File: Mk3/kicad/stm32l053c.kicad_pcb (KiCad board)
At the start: 2 copper layers, 26.7 x 43.2 mm, 34 parts, among them J2 GND, J3 TX, P1 SWD, U1 AP2112, U2 STM32L053C8_LQFP48, U3 ADS1015, U4 UFL_SMA, U5 RFM92/95

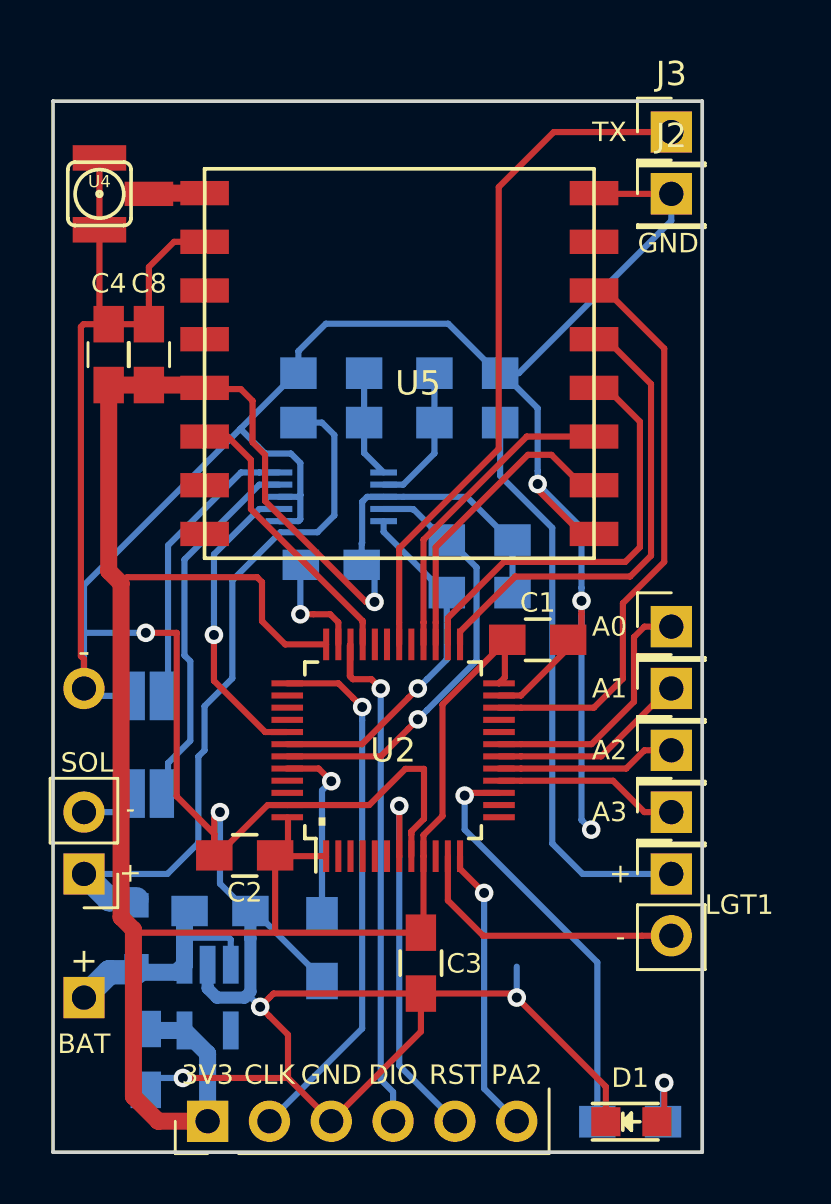
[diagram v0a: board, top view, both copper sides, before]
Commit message: More ground pins
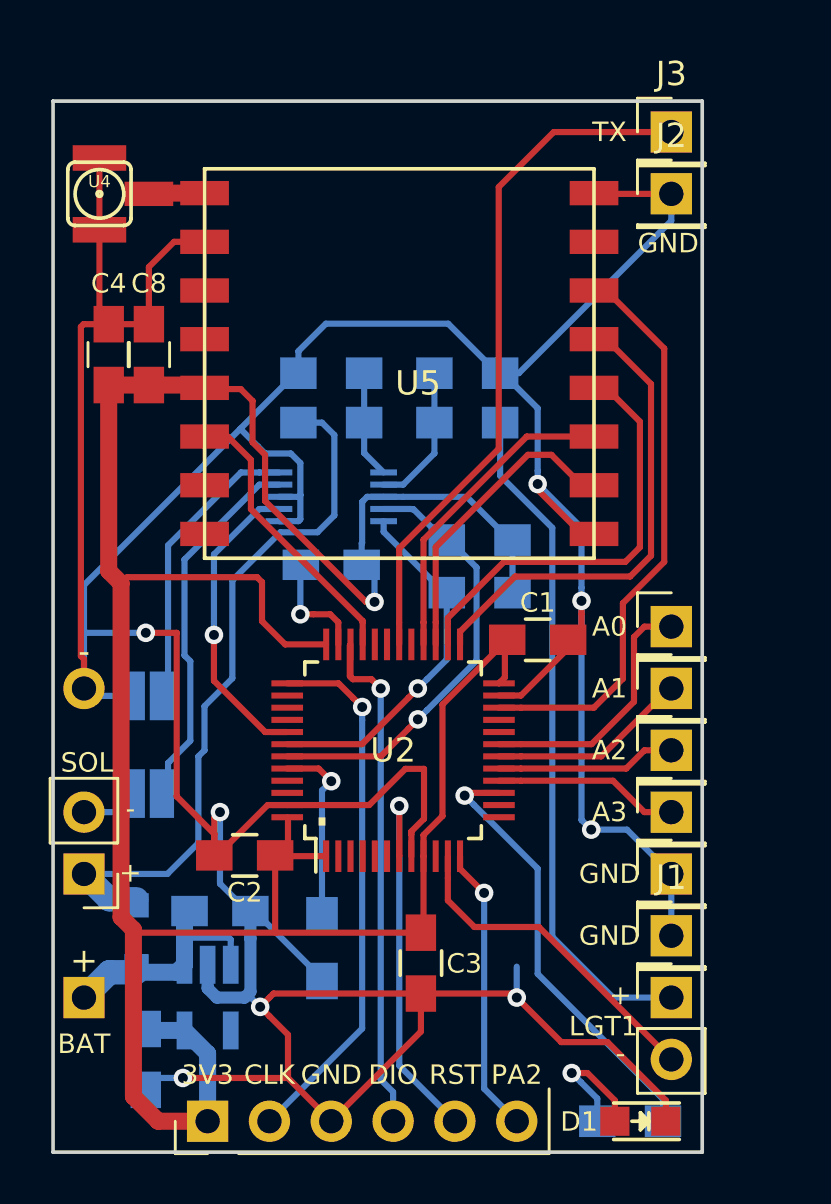
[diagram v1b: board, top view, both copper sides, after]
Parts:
- added J1: GND, Pin_Headers:Pin_Header_Straight_1x01_Pitch2.54mm, F.Cu at (161.3, 86.4)
- added J4: GND, Pin_Headers:Pin_Header_Straight_1x01_Pitch2.54mm, F.Cu at (161.3, 83.8)
- moved LGT1 5.08 mm to (161.3, 88.9)
- moved D1 0.37 mm to (160.0, 94.0), turned to 180 degrees
- turned R1 to 180 degrees
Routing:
- net Earth: track 201.8 -> 210.5 mm
- net Net-(LGT1-Pad1): track 23.6 -> 27.9 mm
- net Net-(D1-Pad2): track 3.35 -> 5.51 mm
- net LGT_GND: track 11.6 -> 13.7 mm
- net LED: track 17.1 -> 18.2 mm

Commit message: Connect all the pins of the RFM95 module
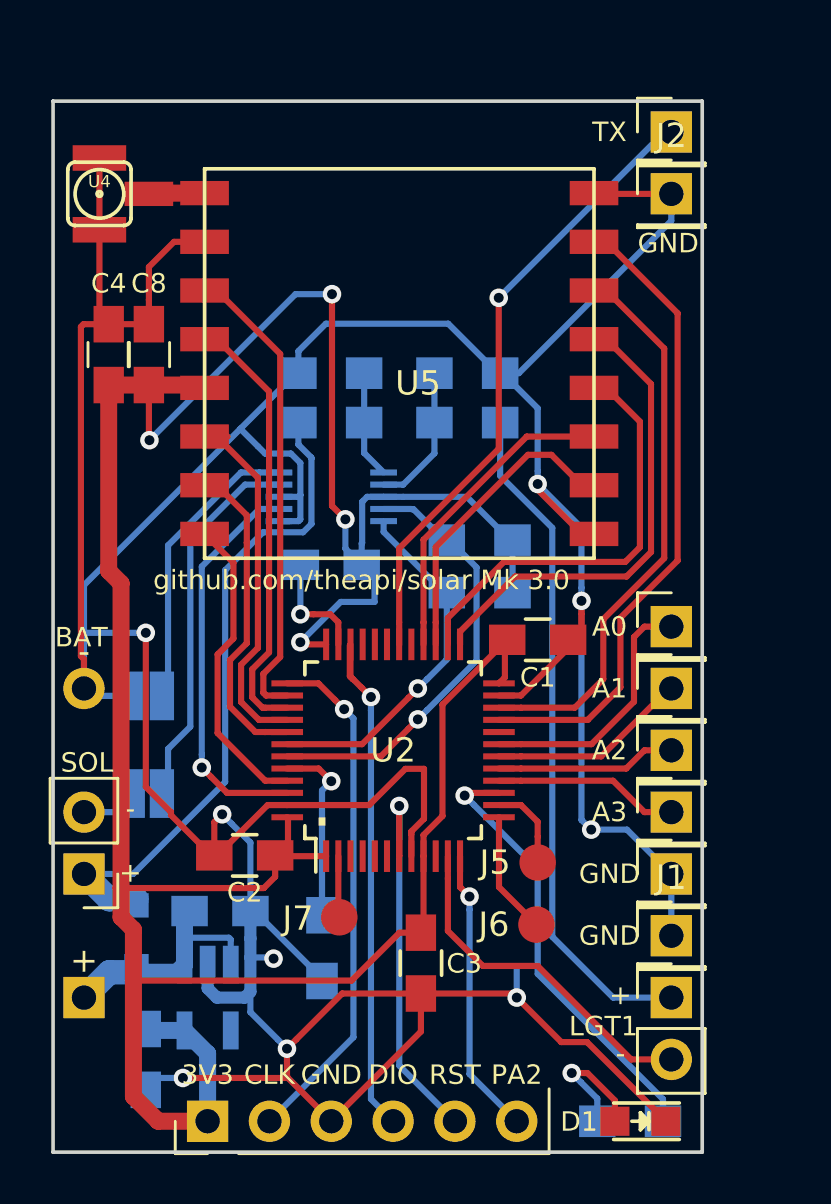
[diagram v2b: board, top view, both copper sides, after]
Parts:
- added J5: TEST_1P, theapi:TestPoint, F.Cu at (155.8, 83.3)
- added J6: TEST_1P, theapi:TestPoint, F.Cu at (155.8, 85.9)
- added J7: TEST_1P, theapi:TestPoint, F.Cu at (147.7, 85.6)
- added REF**: TheApiLogoTiny, theapi:TheApiLogoTiny, F.Cu at (137.2, 90.5)
- added REF**: TheApiLogo, theapi:TheApiLogoSmall, B.Cu at (141.8, 52.8)
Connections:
- net Net-(R4-Pad1) renamed /BOOT0
- U2 pad 13: Net-(U2-Pad13) -> /PA3
- U2 pad 14: Net-(U2-Pad14) -> /PA4
- U2 pad 2: Net-(U2-Pad2) -> /PC13
- U2 pad 21: Net-(U2-Pad21) -> DIO5
- U2 pad 33: DIO0 -> Net-(U2-Pad33)
- U2 pad 38: Net-(U2-Pad38) -> DIO3
- U2 pad 39: Net-(U2-Pad39) -> DIO4
- U2 pad 40: Net-(U2-Pad40) -> DIO0
- U2 pad 41: ADC_RDY -> DIO1
- U2 pad 45: Net-(U2-Pad45) -> DIO2
- U2 pad 46: Net-(U2-Pad46) -> ADC_RDY
- U5 pad 11: Net-(U5-Pad11) -> DIO3
- U5 pad 12: Net-(U5-Pad12) -> DIO4
- U5 pad 15: Net-(U5-Pad15) -> DIO1
- U5 pad 16: Net-(U5-Pad16) -> DIO2
- U5 pad 7: Net-(U5-Pad7) -> DIO5
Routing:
- net DIO5: track 0.00 -> 26.5 mm
- net DIO3: track 0.00 -> 19.4 mm
- net DIO4: track 0.00 -> 18.0 mm
- net DIO1: track 0.00 -> 13.2 mm
- net DIO2: track 0.00 -> 12.6 mm
- net +3V3: track 118.0 -> 129.4 mm, vias 1 -> 4
- net /PA3: track 0.00 -> 5.05 mm
- net ADC_RDY: track 12.5 -> 16.3 mm
- net DIO0: track 11.8 -> 15.5 mm
- net /PA4: track 0.00 -> 3.55 mm
- net USART1_TX: track 28.5 -> 25.8 mm, vias 0 -> 1
- net /PC13: track 0.00 -> 2.66 mm
- net Net-(D2-Pad2): track 29.5 -> 27.4 mm
- net Earth: track 210.5 -> 209.7 mm, vias 9 -> 10
- net SWCLK: track 22.1 -> 21.3 mm
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
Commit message: Extra battery pins
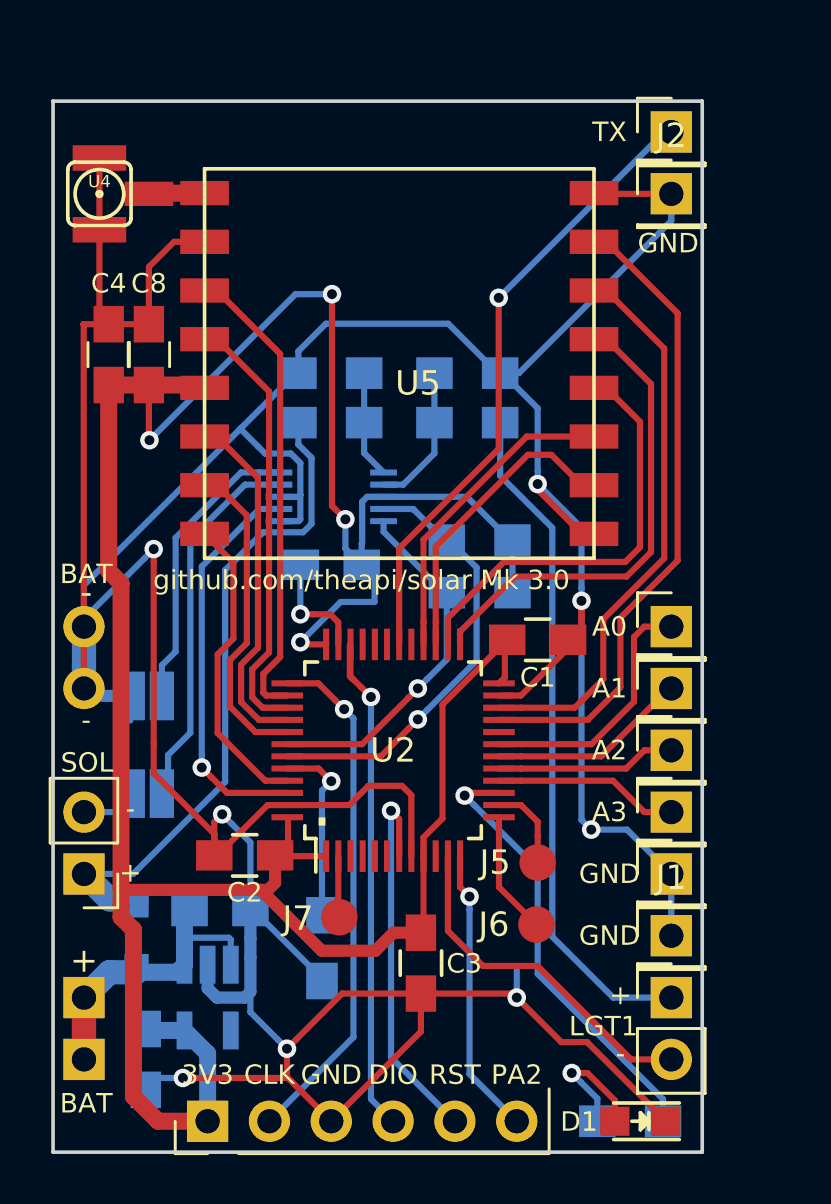
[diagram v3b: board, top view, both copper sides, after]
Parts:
- BT1: footprint theapi:BatteryBox -> theapi:BatteryBoxAndPins
- moved REF** 7.61 mm to (143.0, 85.5)
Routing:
- net Earth: track 209.7 -> 215.3 mm, vias 10 -> 9
- net +3V3: track 129.4 -> 125.4 mm
- net Net-(BT1-Pad1): track 9.97 -> 12.5 mm

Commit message: Serial RX
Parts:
- added J8: RX, Pin_Headers:Pin_Header_Straight_1x01_Pitch2.54mm, F.Cu at (154.9, 53.3)
- moved J3 3.81 mm to (157.5, 53.3)
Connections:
- U2 pad 31: Net-(U2-Pad31) -> USART1_RX
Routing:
- net USART1_RX: track 0.00 -> 23.3 mm, vias 0 -> 1
- net USART1_TX: track 25.8 -> 24.1 mm
- net +3V3: track 125.4 -> 126.8 mm
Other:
- board text added: "RX"
- board text added: "STM32 L053C8T"
- board text added: "U2"

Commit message: An extra capacitor
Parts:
- added C9: 10uF, Capacitors_SMD:C_0805_HandSoldering, F.Cu at (140.3, 86.4)
- moved REF** 1.14 mm to (144.2, 85.8)
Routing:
- net +3V3: track 126.8 -> 125.2 mm
- net Earth: track 215.3 -> 216.2 mm
- net Net-(LGT1-Pad1): track 27.9 -> 27.2 mm

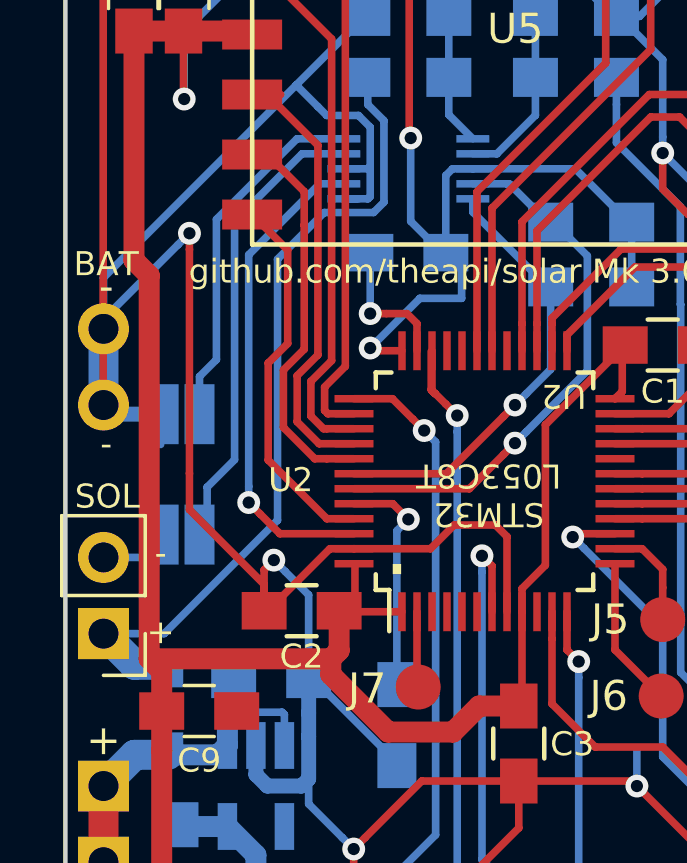
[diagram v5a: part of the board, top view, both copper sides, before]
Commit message: Pullup on ADC RDY pin
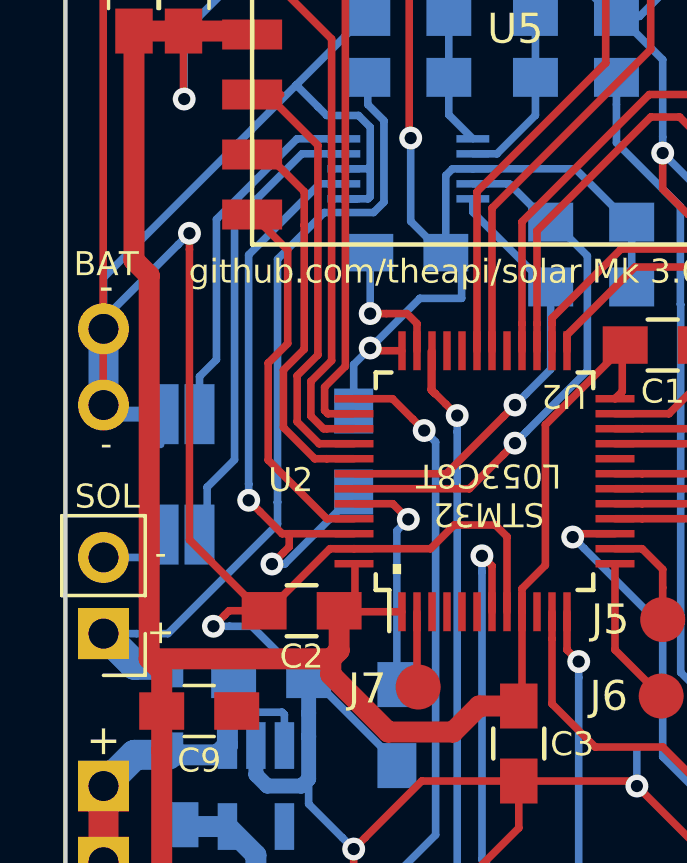
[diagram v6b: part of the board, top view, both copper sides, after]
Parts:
- added R10: 10K, Resistors_SMD:R_0805_HandSoldering, B.Cu at (145.5, 77.8)
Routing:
- net ADC_RDY: track 16.3 -> 21.3 mm, vias 1 -> 2
- net +3V3: track 125.2 -> 127.5 mm
